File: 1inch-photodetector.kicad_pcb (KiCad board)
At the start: 4 copper layers, 25.4 x 25.4 mm, 23 parts, among them J1 Conn_01x03, J2 Conn_Coaxial, U1 ADA4898-2, U2 LT3032IDE-12

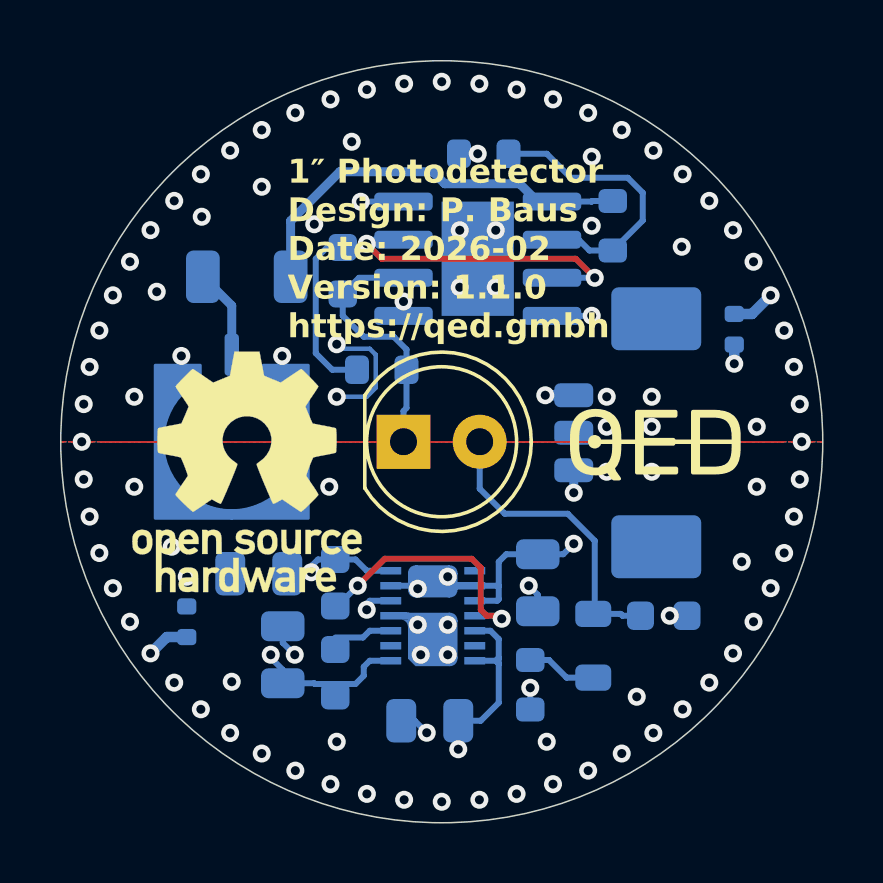
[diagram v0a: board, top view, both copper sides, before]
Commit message: Bump footprints to latest
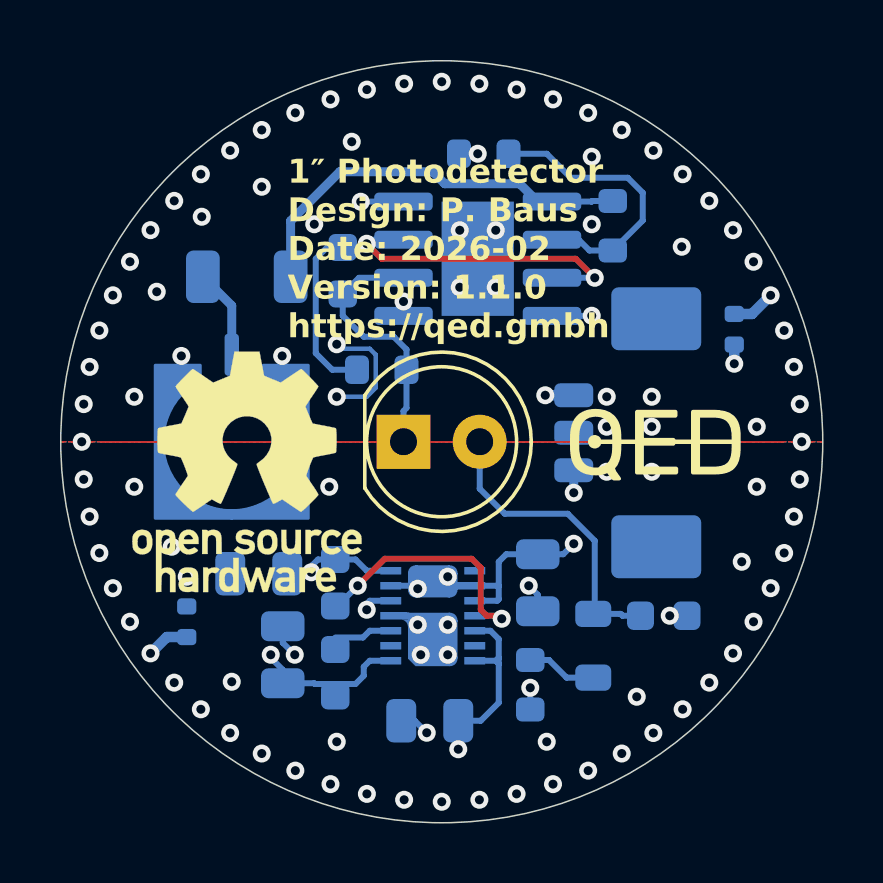
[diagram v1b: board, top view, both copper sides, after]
